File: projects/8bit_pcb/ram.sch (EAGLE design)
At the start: 100 parts, among them IC1 74LS00N

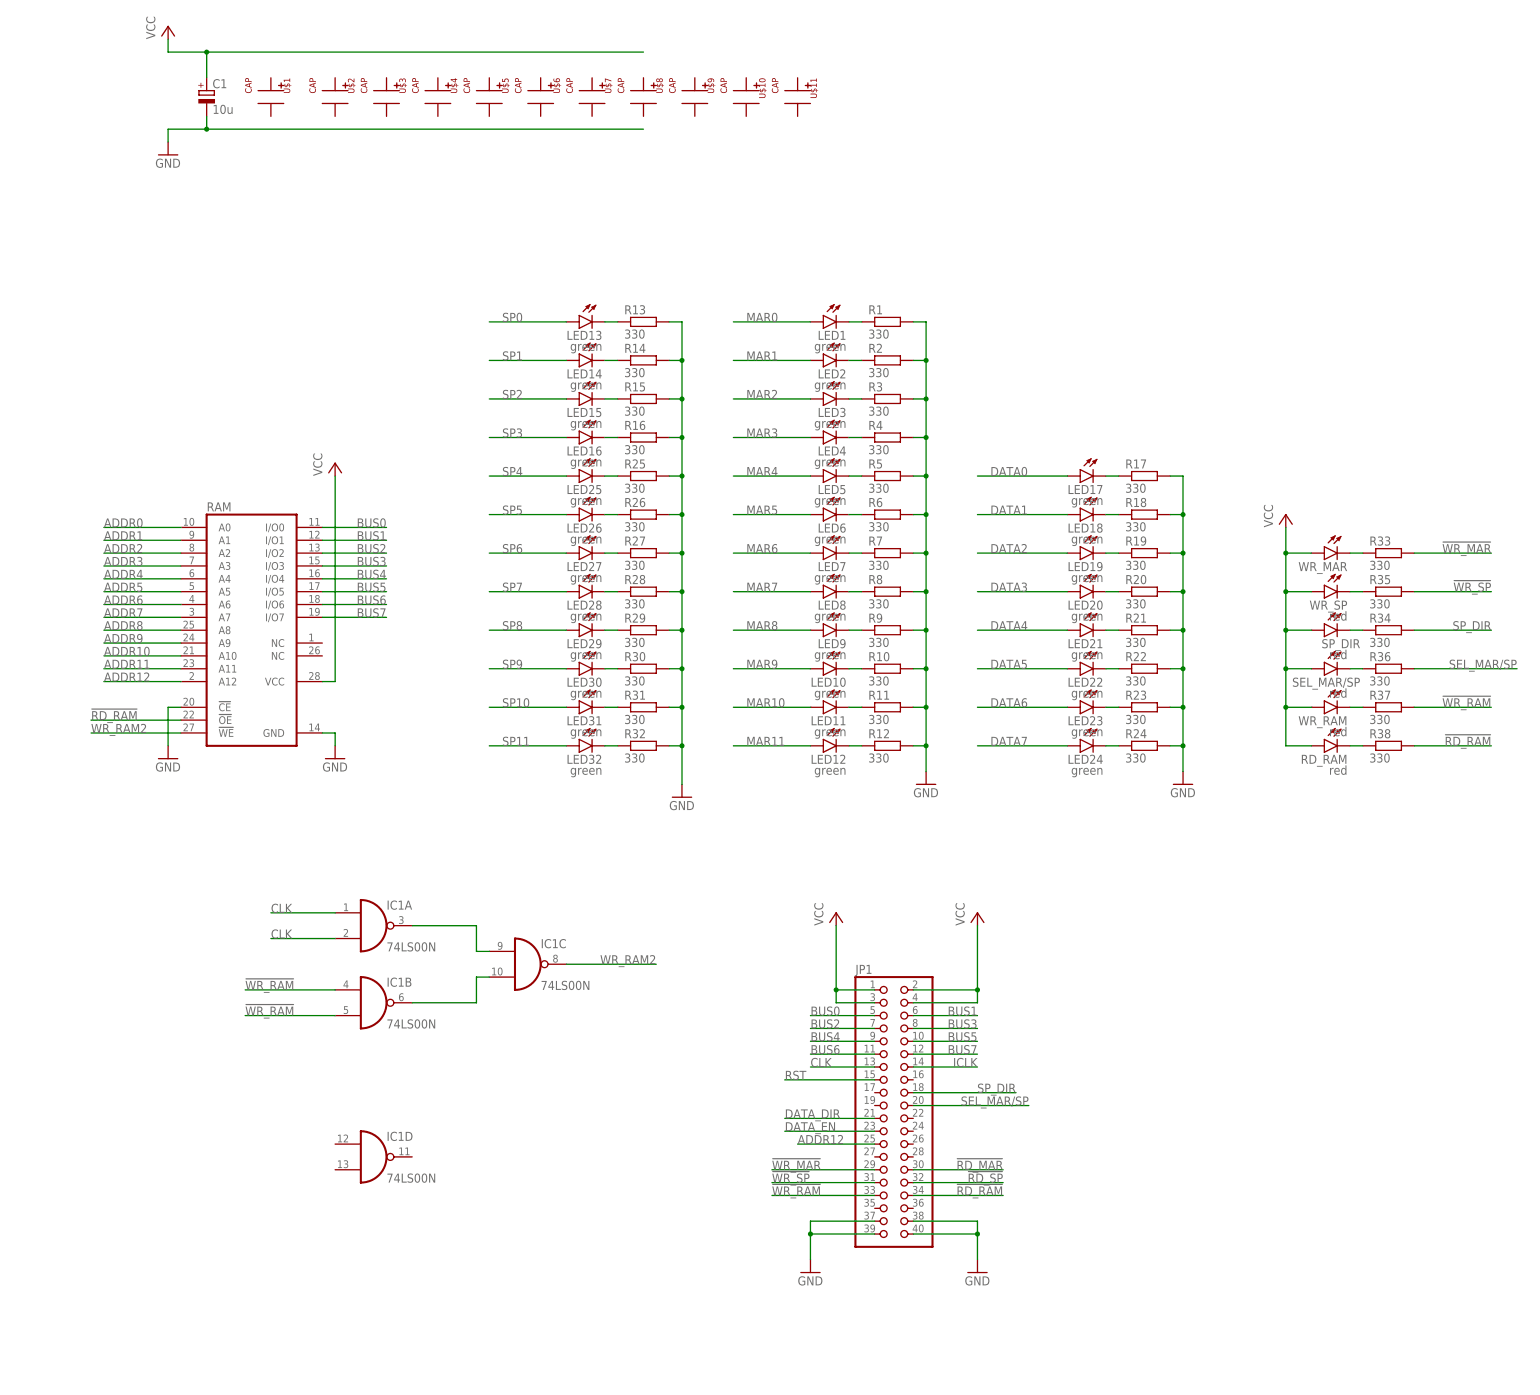
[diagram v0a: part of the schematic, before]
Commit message: RAM, Disp16Seg, Decoder
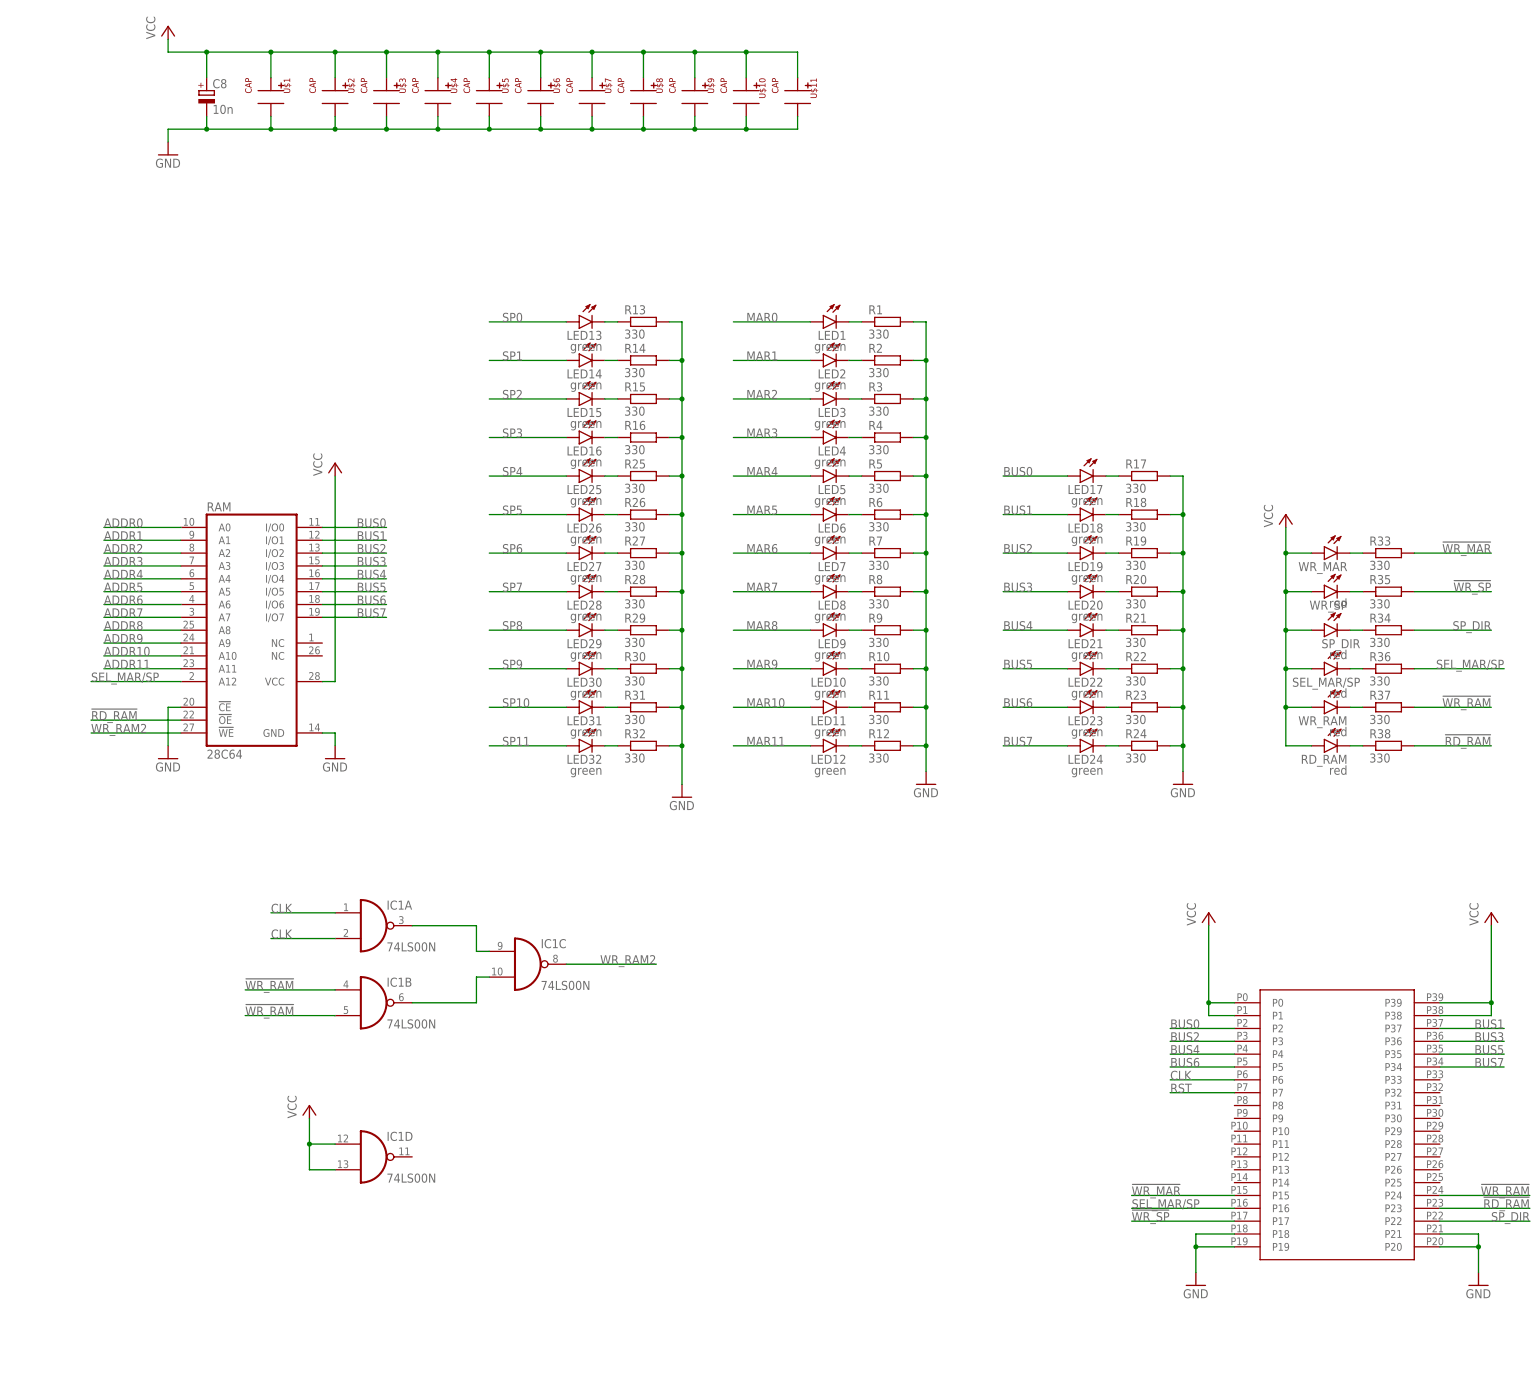
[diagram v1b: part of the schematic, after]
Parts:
- removed C1: 10u, rcl:CPOL-EUE5-8.5
- removed JP1: (no value), pinhead:PINHD-2X20/90
- added C8: 10n, rcl:CPOL-EUE2,5-6E
- added U$12: 2X40, IsaacAlonso:2X40
- RAM: value (none) -> 28C64
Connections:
- removed net !RD_MAR: JP1.30
- removed net !RD_SP: JP1.32
- removed net ADDR12: JP1.25, RAM.A12
- removed net DATA0: LED17.A
- removed net DATA1: LED18.A
- removed net DATA2: LED19.A
- removed net DATA3: LED20.A
- removed net DATA4: LED21.A
- removed net DATA5: LED22.A
- removed net DATA6: LED23.A
- removed net DATA7: LED24.A
- removed net DATA_DIR: JP1.21
- removed net DATA_EN: JP1.23
- removed net ICLK: JP1.14
- net !RD_RAM: now also U$12.P23; no longer JP1.34
- net !WR_MAR: now also U$12.P15; no longer JP1.29
- net !WR_RAM: now also U$12.P24; no longer JP1.33
- net !WR_SP: now also U$12.P17; no longer JP1.31
- net BUS0: now also LED17.A, U$12.P2; no longer JP1.5
- net BUS1: now also LED18.A, U$12.P37; no longer JP1.6
- net BUS2: now also LED19.A, U$12.P3; no longer JP1.7
- net BUS3: now also LED20.A, U$12.P36; no longer JP1.8
- net BUS4: now also LED21.A, U$12.P4; no longer JP1.9
- net BUS5: now also LED22.A, U$12.P35; no longer JP1.10
- net BUS6: now also LED23.A, U$12.P5; no longer JP1.11
- net BUS7: now also LED24.A, U$12.P34; no longer JP1.12
- net CLK: now also U$12.P6; no longer JP1.13
- net GND: now also C8.-, U$1.P-, U$10.P-, U$11.P-, U$12.P18, U$12.P19, U$12.P20, U$12.P21, U$2.P-, U$3.P-, U$4.P-, U$5.P-, U$6.P-, U$7.P-, U$8.P-, U$9.P-; no longer C1.-, JP1.37, JP1.38, JP1.39, JP1.40
- net RST: now also U$12.P7; no longer JP1.15
- net SEL_MAR/SP: now also RAM.A12, U$12.P16; no longer JP1.20
- net SP_DIR: now also U$12.P22; no longer JP1.18
- net VCC: now also C8.+, IC1D.I0, IC1D.I1, U$1.P+, U$10.P+, U$11.P+, U$12.P0, U$12.P1, U$12.P38, U$12.P39, U$2.P+, U$3.P+, U$4.P+, U$5.P+, U$6.P+, U$7.P+, U$8.P+, U$9.P+; no longer C1.+, JP1.1, JP1.2, JP1.3, JP1.4
